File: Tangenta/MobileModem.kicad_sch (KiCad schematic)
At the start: 12 parts, among them J7 1-2199230-5, J8 HYC90-SIM06-180

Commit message: Fixes, continued...
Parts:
- C70, C71, C72: symbol C_Small:C_Small -> Device:C_Small
- H10, H11: symbol MountingHole:MountingHole -> Mechanical:MountingHole
- R42, R43, R44, R45, R46: symbol R_Small_US:R_Small_US -> Device:R_Small_US
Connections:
- net 3V3: no longer R44.1
- net GNDREF: no longer C71.1, C72.1, R42.1, R43.1, R45.1
- net UIM1_CLK: no longer C70.2
- net UIM1_DATA: no longer R46.1
- net UIM1_PWR: no longer C71.2, C72.2, R46.2
- net at J7.21: no longer R42.2
- net at J7.6: no longer R44.2
- net at J7.69: no longer R43.2
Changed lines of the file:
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@@
 	)
 	(symbol
-		(lib_id "MountingHole:MountingHole")
+		(lib_id "Mechanical:MountingHole")
 		(at 186.055 76.2 0)
 		(unit 1)
@@
 	)
 	(symbol
-		(lib_id "C_Small:C_Small")
+		(lib_id "Device:C_Small")
 		(at 140.97 68.58 180)
 		(unit 1)
@@
 	)
 	(symbol
-		(lib_id "C_Small:C_Small")
+		(lib_id "Device:C_Small")
 		(at 156.21 68.58 180)
 		(unit 1)
@@
 	)
 	(symbol
-		(lib_id "R_Small_US:R_Small_US")
+		(lib_id "Device:R_Small_US")
 		(at 173.99 74.93 180)
 		(unit 1)
@@
 	)
 	(symbol
-		(lib_id "R_Small_US:R_Small_US")
+		(lib_id "Device:R_Small_US")
 		(at 54.61 77.47 90)
 		(unit 1)
@@
 	)
 	(symbol
-		(lib_id "C_Small:C_Small")
+		(lib_id "Device:C_Small")
 		(at 124.46 95.25 180)
 		(unit 1)
@@
 	)
 	(symbol
-		(lib_id "MountingHole:MountingHole")
+		(lib_id "Mechanical:MountingHole")
 		(at 186.055 83.82 0)
 		(unit 1)
@@
 	)
 	(symbol
-		(lib_id "R_Small_US:R_Small_US")
+		(lib_id "Device:R_Small_US")
 		(at 92.71 57.15 270)
 		(mirror x)
@@
 	)
 	(symbol
-		(lib_id "R_Small_US:R_Small_US")
+		(lib_id "Device:R_Small_US")
 		(at 54.61 128.27 90)
 		(unit 1)
@@
 	)
 	(symbol
-		(lib_id "R_Small_US:R_Small_US")
+		(lib_id "Device:R_Small_US")
 		(at 124.46 104.14 180)
 		(unit 1)

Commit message: Fixes, continued...
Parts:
- C70, C71, C72: symbol Device:C_Small -> C_Small:C_Small
- H10, H11: symbol Mechanical:MountingHole -> MountingHole:MountingHole
- J8: footprint SIM-SMD_HYC90-SIM06-180:SIM-SMD_HYC90-SIM06-180 -> SIM_Holder:SIM-SMD_HYC90-SIM06-180
- R42, R43, R44, R45, R46: symbol Device:R_Small_US -> R_Small_US:R_Small_US
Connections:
- net 3V3: now also R44.1
- net GNDREF: now also C71.1, C72.1, R42.1, R43.1, R45.1
- net UIM1_CLK: now also C70.2
- net UIM1_DATA: now also R46.1
- net UIM1_PWR: now also C71.2, C72.2, R46.2
- net at J7.21: now also R42.2
- net at J7.6: now also R44.2
- net at J7.69: now also R43.2
- new net: C70.1, R45.2
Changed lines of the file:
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@@
 			)
 		)
-		(property "Footprint" "SIM-SMD_HYC90-SIM06-180:SIM-SMD_HYC90-SIM06-180"
+		(property "Footprint" "SIM_Holder:SIM-SMD_HYC90-SIM06-180"
 			(at 149.86 80.01 0)
 			(effects
@@
 	)
 	(symbol
-		(lib_id "Mechanical:MountingHole")
+		(lib_id "MountingHole:MountingHole")
 		(at 186.055 76.2 0)
 		(unit 1)
@@
 	)
 	(symbol
-		(lib_id "Device:C_Small")
+		(lib_id "C_Small:C_Small")
 		(at 140.97 68.58 180)
 		(unit 1)
@@
 	)
 	(symbol
-		(lib_id "Device:C_Small")
+		(lib_id "C_Small:C_Small")
 		(at 156.21 68.58 180)
 		(unit 1)
@@
 	)
 	(symbol
-		(lib_id "Device:R_Small_US")
+		(lib_id "R_Small_US:R_Small_US")
 		(at 173.99 74.93 180)
 		(unit 1)
@@
 	)
 	(symbol
-		(lib_id "Device:R_Small_US")
+		(lib_id "R_Small_US:R_Small_US")
 		(at 54.61 77.47 90)
 		(unit 1)
@@
 	)
 	(symbol
-		(lib_id "Device:C_Small")
+		(lib_id "C_Small:C_Small")
 		(at 124.46 95.25 180)
 		(unit 1)
@@
 	)
 	(symbol
-		(lib_id "Mechanical:MountingHole")
+		(lib_id "MountingHole:MountingHole")
 		(at 186.055 83.82 0)
 		(unit 1)
@@
 	)
 	(symbol
-		(lib_id "Device:R_Small_US")
+		(lib_id "R_Small_US:R_Small_US")
 		(at 92.71 57.15 270)
 		(mirror x)
@@
 	)
 	(symbol
-		(lib_id "Device:R_Small_US")
+		(lib_id "R_Small_US:R_Small_US")
 		(at 54.61 128.27 90)
 		(unit 1)
@@
 	)
 	(symbol
-		(lib_id "Device:R_Small_US")
+		(lib_id "R_Small_US:R_Small_US")
 		(at 124.46 104.14 180)
 		(unit 1)

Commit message: Fixes, before checks.
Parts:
- C70, C71, C72: symbol C_Small:C_Small -> Device:C_Small
- H10, H11: symbol MountingHole:MountingHole -> Mechanical:MountingHole
- J7: symbol 1-2199230-5:1-2199230-5 -> M2_Slot:1-2199230-5
- J8: symbol HYC90-SIM06-180:HYC90-SIM06-180 -> SIM_Holder:HYC90-SIM06-180
- R42, R43, R44, R45, R46: symbol R_Small_US:R_Small_US -> Device:R_Small_US
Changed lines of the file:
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@@
 	)
 	(symbol
-		(lib_id "HYC90-SIM06-180:HYC90-SIM06-180")
+		(lib_id "SIM_Holder:HYC90-SIM06-180")
 		(at 148.59 87.63 0)
 		(unit 1)
@@
 	)
 	(symbol
-		(lib_id "MountingHole:MountingHole")
+		(lib_id "Mechanical:MountingHole")
 		(at 186.055 76.2 0)
 		(unit 1)
@@
 	)
 	(symbol
-		(lib_id "C_Small:C_Small")
+		(lib_id "Device:C_Small")
 		(at 140.97 68.58 180)
 		(unit 1)
@@
 	)
 	(symbol
-		(lib_id "C_Small:C_Small")
+		(lib_id "Device:C_Small")
 		(at 156.21 68.58 180)
 		(unit 1)
@@
 	)
 	(symbol
-		(lib_id "R_Small_US:R_Small_US")
+		(lib_id "Device:R_Small_US")
 		(at 173.99 74.93 180)
 		(unit 1)
@@
 	)
 	(symbol
-		(lib_id "R_Small_US:R_Small_US")
+		(lib_id "Device:R_Small_US")
 		(at 54.61 77.47 90)
 		(unit 1)
@@
 	)
 	(symbol
-		(lib_id "C_Small:C_Small")
+		(lib_id "Device:C_Small")
 		(at 124.46 95.25 180)
 		(unit 1)
@@
 	)
 	(symbol
-		(lib_id "MountingHole:MountingHole")
+		(lib_id "Mechanical:MountingHole")
 		(at 186.055 83.82 0)
 		(unit 1)
@@
 	)
 	(symbol
-		(lib_id "R_Small_US:R_Small_US")
+		(lib_id "Device:R_Small_US")
 		(at 92.71 57.15 270)
 		(mirror x)
@@
 	)
 	(symbol
-		(lib_id "R_Small_US:R_Small_US")
+		(lib_id "Device:R_Small_US")
 		(at 54.61 128.27 90)
 		(unit 1)
@@
 	)
 	(symbol
-		(lib_id "R_Small_US:R_Small_US")
+		(lib_id "Device:R_Small_US")
 		(at 124.46 104.14 180)
 		(unit 1)
@@
 	)
 	(symbol
-		(lib_id "1-2199230-5:1-2199230-5")
+		(lib_id "M2_Slot:1-2199230-5")
 		(at 73.66 44.45 90)
 		(mirror x)

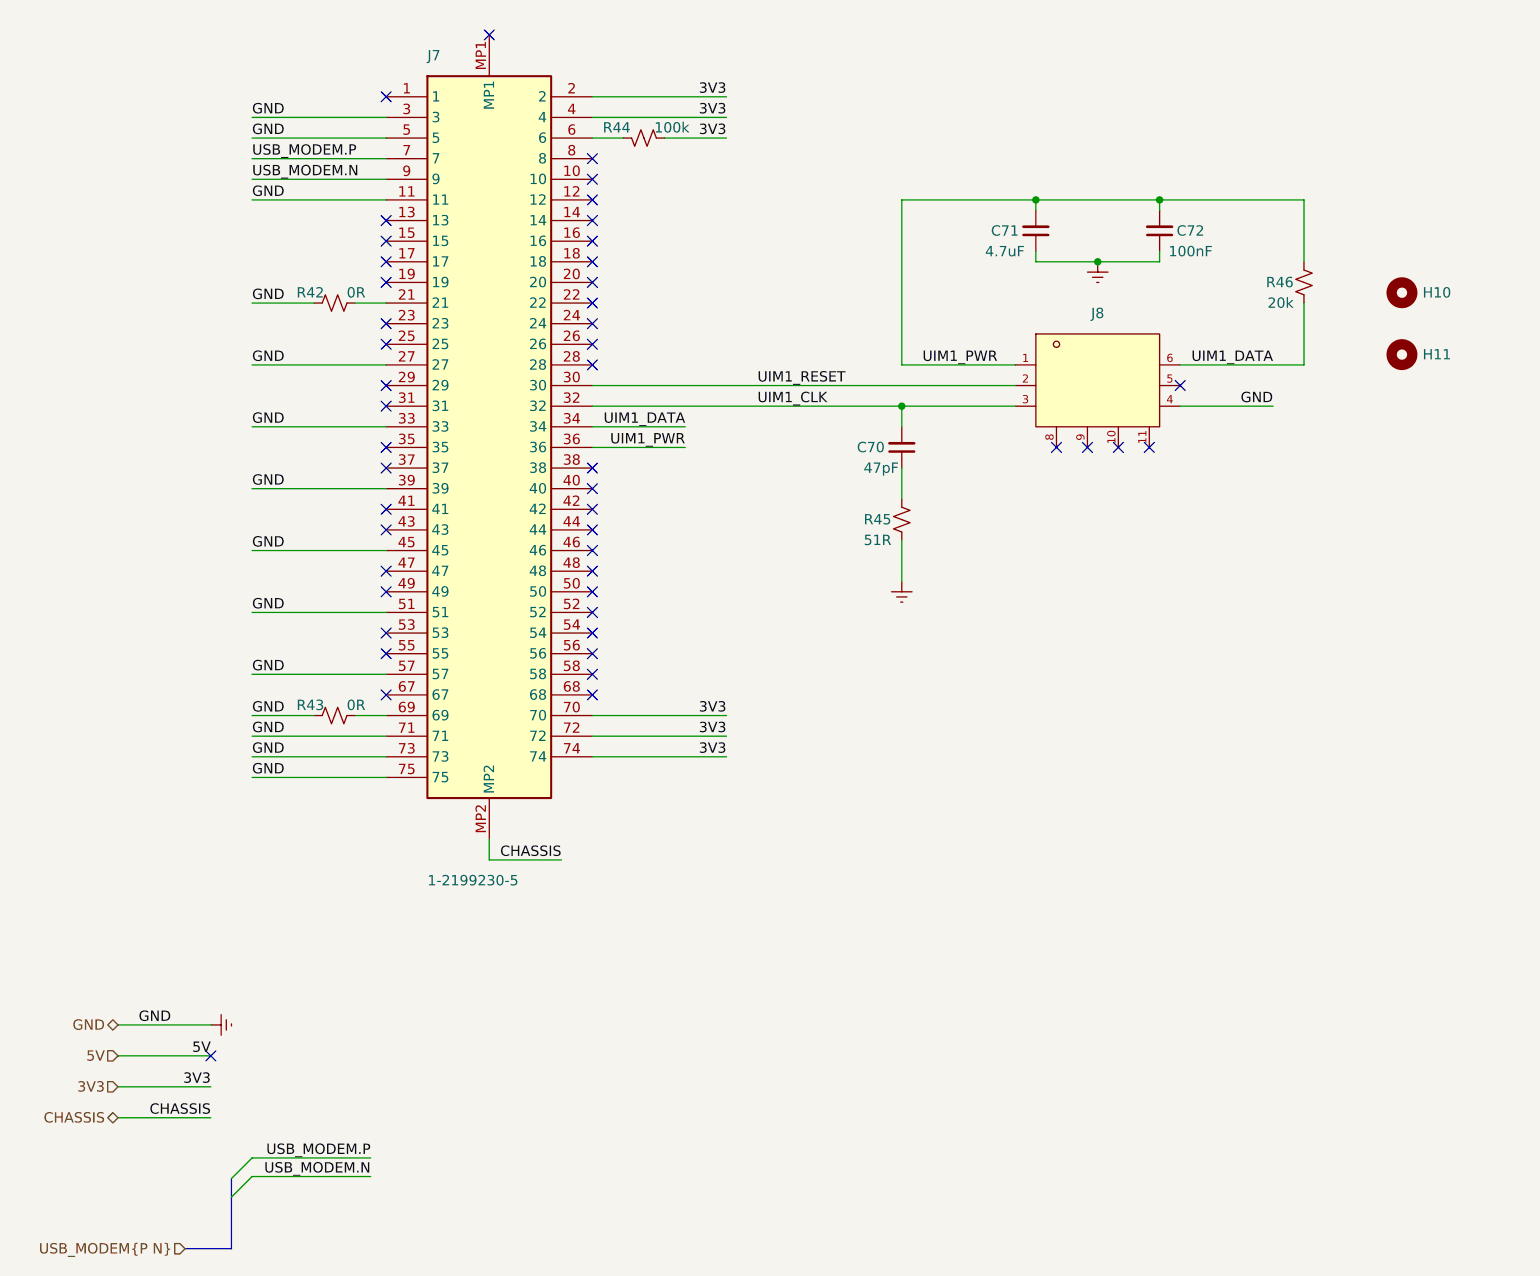
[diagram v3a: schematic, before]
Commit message: Reverting to the original design.
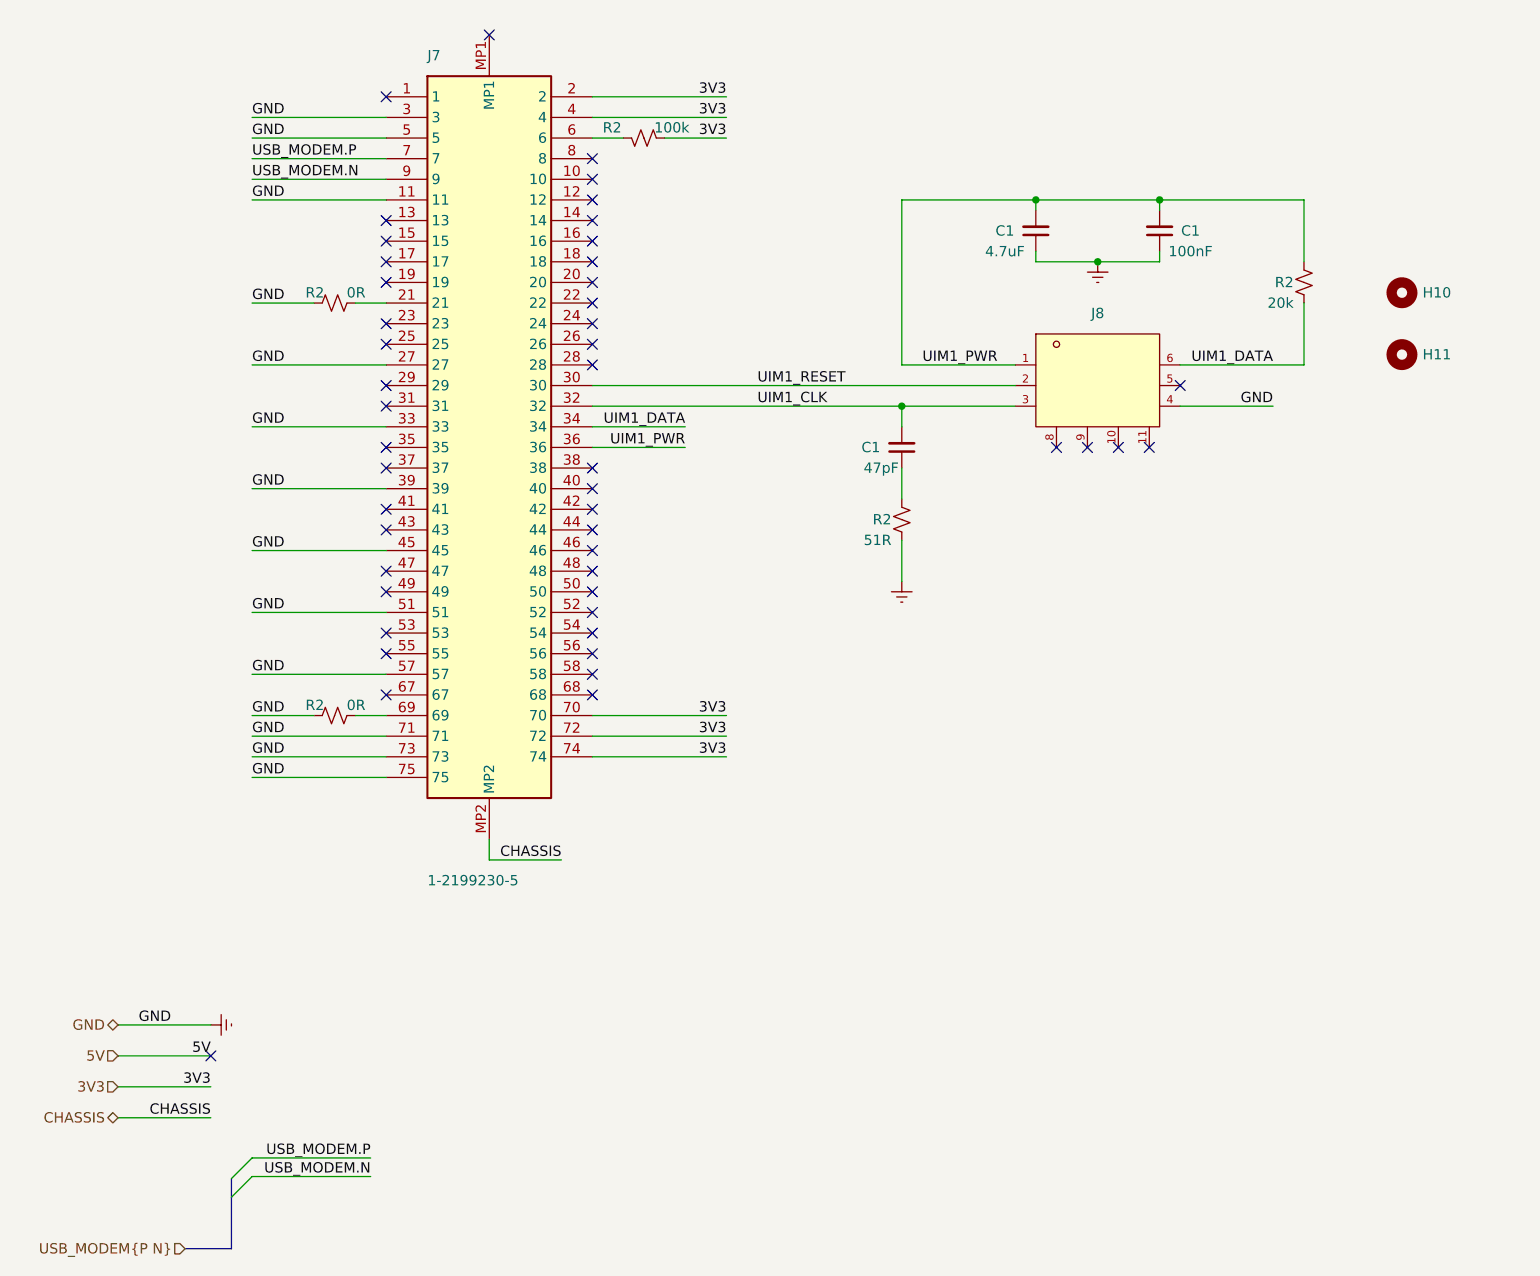
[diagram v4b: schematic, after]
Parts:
- C1: renamed from C71; symbol Device:C_Small -> CholaSymbolsPrjLib:C_Small
- C1: renamed from C72; symbol Device:C_Small -> CholaSymbolsPrjLib:C_Small
- C1: renamed from C70; symbol Device:C_Small -> CholaSymbolsPrjLib:C_Small
- H10, H11: symbol Mechanical:MountingHole -> CholaSymbolsPrjLib:MountingHole
- J7: symbol M2_Slot:1-2199230-5 -> CholaSymbolsPrjLib:1-2199230-5
- J8: symbol SIM_Holder:HYC90-SIM06-180 -> CholaSymbolsPrjLib:HYC90-SIM06-180
- R2: renamed from R46; symbol Device:R_Small_US -> CholaSymbolsPrjLib:R_Small_US
- R2: renamed from R42; symbol Device:R_Small_US -> CholaSymbolsPrjLib:R_Small_US
- R2: renamed from R44; symbol Device:R_Small_US -> CholaSymbolsPrjLib:R_Small_US
- R2: renamed from R43; symbol Device:R_Small_US -> CholaSymbolsPrjLib:R_Small_US
- R2: renamed from R45; symbol Device:R_Small_US -> CholaSymbolsPrjLib:R_Small_US

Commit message: ...
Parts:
- C1: symbol CholaSymbolsPrjLib:C_Small -> LocalPrjLib:C_Small
- H10, H11: symbol CholaSymbolsPrjLib:MountingHole -> LocalPrjLib:MountingHole
- J7: symbol CholaSymbolsPrjLib:1-2199230-5 -> LocalPrjLib:1-2199230-5
- J8: symbol CholaSymbolsPrjLib:HYC90-SIM06-180 -> LocalPrjLib:HYC90-SIM06-180
- R2: symbol CholaSymbolsPrjLib:R_Small_US -> LocalPrjLib:R_Small_US
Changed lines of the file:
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@@
     (effects (font (size 1.27 1.27)) (justify right))
   )
-  (symbol (lib_id "CholaSymbolsPrjLib:HYC90-SIM06-180") (at 148.59 87.63 0) (unit 1)
+  (symbol (lib_id "LocalPrjLib:HYC90-SIM06-180") (at 148.59 87.63 0) (unit 1)
     (in_bom yes) (on_board yes) (dnp no) (fields_autoplaced)
     (property "Reference" "J8" (at 148.59 78.74 0)
@@
     )
   )
-  (symbol (lib_id "CholaSymbolsPrjLib:MountingHole") (at 186.055 76.2 0) (unit 1)
+  (symbol (lib_id "LocalPrjLib:MountingHole") (at 186.055 76.2 0) (unit 1)
     (in_bom yes) (on_board yes) (dnp no)
     (property "Reference" "H10" (at 188.595 76.2 0)
@@
     )
   )
-  (symbol (lib_id "CholaSymbolsPrjLib:C_Small") (at 140.97 68.58 180) (unit 1)
+  (symbol (lib_id "LocalPrjLib:C_Small") (at 140.97 68.58 180) (unit 1)
     (in_bom yes) (on_board yes) (dnp no)
     (property "Reference" "C1" (at 137.16 68.58 0)
@@
     )
   )
-  (symbol (lib_id "CholaSymbolsPrjLib:C_Small") (at 156.21 68.58 180) (unit 1)
+  (symbol (lib_id "LocalPrjLib:C_Small") (at 156.21 68.58 180) (unit 1)
     (in_bom yes) (on_board yes) (dnp no)
     (property "Reference" "C1" (at 160.02 68.58 0)
@@
     )
   )
-  (symbol (lib_id "CholaSymbolsPrjLib:R_Small_US") (at 173.99 74.93 180) (unit 1)
+  (symbol (lib_id "LocalPrjLib:R_Small_US") (at 173.99 74.93 180) (unit 1)
     (in_bom yes) (on_board yes) (dnp no)
     (property "Reference" "R2" (at 172.72 74.93 0)
@@
     )
   )
-  (symbol (lib_id "CholaSymbolsPrjLib:R_Small_US") (at 54.61 77.47 90) (unit 1)
+  (symbol (lib_id "LocalPrjLib:R_Small_US") (at 54.61 77.47 90) (unit 1)
     (in_bom yes) (on_board yes) (dnp no)
     (property "Reference" "R2" (at 53.34 76.2 90)
@@
     )
   )
-  (symbol (lib_id "CholaSymbolsPrjLib:C_Small") (at 124.46 95.25 180) (unit 1)
+  (symbol (lib_id "LocalPrjLib:C_Small") (at 124.46 95.25 180) (unit 1)
     (in_bom yes) (on_board yes) (dnp no)
     (property "Reference" "C1" (at 120.65 95.25 0)
@@
     )
   )
-  (symbol (lib_id "CholaSymbolsPrjLib:MountingHole") (at 186.055 83.82 0) (unit 1)
+  (symbol (lib_id "LocalPrjLib:MountingHole") (at 186.055 83.82 0) (unit 1)
     (in_bom yes) (on_board yes) (dnp no)
     (property "Reference" "H11" (at 188.595 83.82 0)
@@
     )
   )
-  (symbol (lib_id "CholaSymbolsPrjLib:R_Small_US") (at 92.71 57.15 270) (mirror x) (unit 1)
+  (symbol (lib_id "LocalPrjLib:R_Small_US") (at 92.71 57.15 270) (mirror x) (unit 1)
     (in_bom yes) (on_board yes) (dnp no)
     (property "Reference" "R2" (at 87.63 55.88 90)
@@
     )
   )
-  (symbol (lib_id "CholaSymbolsPrjLib:R_Small_US") (at 54.61 128.27 90) (unit 1)
+  (symbol (lib_id "LocalPrjLib:R_Small_US") (at 54.61 128.27 90) (unit 1)
     (in_bom yes) (on_board yes) (dnp no)
     (property "Reference" "R2" (at 53.34 127 90)
@@
     )
   )
-  (symbol (lib_id "CholaSymbolsPrjLib:R_Small_US") (at 124.46 104.14 180) (unit 1)
+  (symbol (lib_id "LocalPrjLib:R_Small_US") (at 124.46 104.14 180) (unit 1)
     (in_bom yes) (on_board yes) (dnp no)
     (property "Reference" "R2" (at 123.19 104.14 0)
@@
     )
   )
-  (symbol (lib_id "CholaSymbolsPrjLib:1-2199230-5") (at 73.66 44.45 90) (mirror x) (unit 1)
+  (symbol (lib_id "LocalPrjLib:1-2199230-5") (at 73.66 44.45 90) (mirror x) (unit 1)
     (in_bom yes) (on_board yes) (dnp no)
     (property "Reference" "J7" (at 66.04 46.99 90)

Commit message: Fixes, new approach.
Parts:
- C1: symbol LocalPrjLib:C_Small -> LocalSymbolsPrjLib:C_Small
- H10, H11: symbol LocalPrjLib:MountingHole -> LocalSymbolsPrjLib:MountingHole
- J7: symbol LocalPrjLib:1-2199230-5 -> LocalSymbolsPrjLib:1-2199230-5
- J8: symbol LocalPrjLib:HYC90-SIM06-180 -> LocalSymbolsPrjLib:HYC90-SIM06-180
- R2: symbol LocalPrjLib:R_Small_US -> LocalSymbolsPrjLib:R_Small_US
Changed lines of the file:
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@@
     (effects (font (size 1.27 1.27)) (justify right))
   )
-  (symbol (lib_id "LocalPrjLib:HYC90-SIM06-180") (at 148.59 87.63 0) (unit 1)
+  (symbol (lib_id "LocalSymbolsPrjLib:HYC90-SIM06-180") (at 148.59 87.63 0) (unit 1)
     (in_bom yes) (on_board yes) (dnp no) (fields_autoplaced)
     (property "Reference" "J8" (at 148.59 78.74 0)
@@
     )
   )
-  (symbol (lib_id "LocalPrjLib:MountingHole") (at 186.055 76.2 0) (unit 1)
+  (symbol (lib_id "LocalSymbolsPrjLib:MountingHole") (at 186.055 76.2 0) (unit 1)
     (in_bom yes) (on_board yes) (dnp no)
     (property "Reference" "H10" (at 188.595 76.2 0)
@@
     )
   )
-  (symbol (lib_id "LocalPrjLib:C_Small") (at 140.97 68.58 180) (unit 1)
+  (symbol (lib_id "LocalSymbolsPrjLib:C_Small") (at 140.97 68.58 180) (unit 1)
     (in_bom yes) (on_board yes) (dnp no)
     (property "Reference" "C1" (at 137.16 68.58 0)
@@
     )
   )
-  (symbol (lib_id "LocalPrjLib:C_Small") (at 156.21 68.58 180) (unit 1)
+  (symbol (lib_id "LocalSymbolsPrjLib:C_Small") (at 156.21 68.58 180) (unit 1)
     (in_bom yes) (on_board yes) (dnp no)
     (property "Reference" "C1" (at 160.02 68.58 0)
@@
     )
   )
-  (symbol (lib_id "LocalPrjLib:R_Small_US") (at 173.99 74.93 180) (unit 1)
+  (symbol (lib_id "LocalSymbolsPrjLib:R_Small_US") (at 173.99 74.93 180) (unit 1)
     (in_bom yes) (on_board yes) (dnp no)
     (property "Reference" "R2" (at 172.72 74.93 0)
@@
     )
   )
-  (symbol (lib_id "LocalPrjLib:R_Small_US") (at 54.61 77.47 90) (unit 1)
+  (symbol (lib_id "LocalSymbolsPrjLib:R_Small_US") (at 54.61 77.47 90) (unit 1)
     (in_bom yes) (on_board yes) (dnp no)
     (property "Reference" "R2" (at 53.34 76.2 90)
@@
     )
   )
-  (symbol (lib_id "LocalPrjLib:C_Small") (at 124.46 95.25 180) (unit 1)
+  (symbol (lib_id "LocalSymbolsPrjLib:C_Small") (at 124.46 95.25 180) (unit 1)
     (in_bom yes) (on_board yes) (dnp no)
     (property "Reference" "C1" (at 120.65 95.25 0)
@@
     )
   )
-  (symbol (lib_id "LocalPrjLib:MountingHole") (at 186.055 83.82 0) (unit 1)
+  (symbol (lib_id "LocalSymbolsPrjLib:MountingHole") (at 186.055 83.82 0) (unit 1)
     (in_bom yes) (on_board yes) (dnp no)
     (property "Reference" "H11" (at 188.595 83.82 0)
@@
     )
   )
-  (symbol (lib_id "LocalPrjLib:R_Small_US") (at 92.71 57.15 270) (mirror x) (unit 1)
+  (symbol (lib_id "LocalSymbolsPrjLib:R_Small_US") (at 92.71 57.15 270) (mirror x) (unit 1)
     (in_bom yes) (on_board yes) (dnp no)
     (property "Reference" "R2" (at 87.63 55.88 90)
@@
     )
   )
-  (symbol (lib_id "LocalPrjLib:R_Small_US") (at 54.61 128.27 90) (unit 1)
+  (symbol (lib_id "LocalSymbolsPrjLib:R_Small_US") (at 54.61 128.27 90) (unit 1)
     (in_bom yes) (on_board yes) (dnp no)
     (property "Reference" "R2" (at 53.34 127 90)
@@
     )
   )
-  (symbol (lib_id "LocalPrjLib:R_Small_US") (at 124.46 104.14 180) (unit 1)
+  (symbol (lib_id "LocalSymbolsPrjLib:R_Small_US") (at 124.46 104.14 180) (unit 1)
     (in_bom yes) (on_board yes) (dnp no)
     (property "Reference" "R2" (at 123.19 104.14 0)
@@
     )
   )
-  (symbol (lib_id "LocalPrjLib:1-2199230-5") (at 73.66 44.45 90) (mirror x) (unit 1)
+  (symbol (lib_id "LocalSymbolsPrjLib:1-2199230-5") (at 73.66 44.45 90) (mirror x) (unit 1)
     (in_bom yes) (on_board yes) (dnp no)
     (property "Reference" "J7" (at 66.04 46.99 90)

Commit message: Fixes...
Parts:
- renumbered C1 to C70, C1 to C71, C1 to C72, R2 to R42, R2 to R43, R2 to R44, R2 to R45, R2 to R46
